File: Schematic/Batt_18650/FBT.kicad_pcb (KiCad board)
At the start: 2 copper layers, 42.8 x 122.5 mm, 19 parts, among them J1 TRRS Connector 3.5, J2 TRRS Connector 3.5, SW1 SW_SPDT

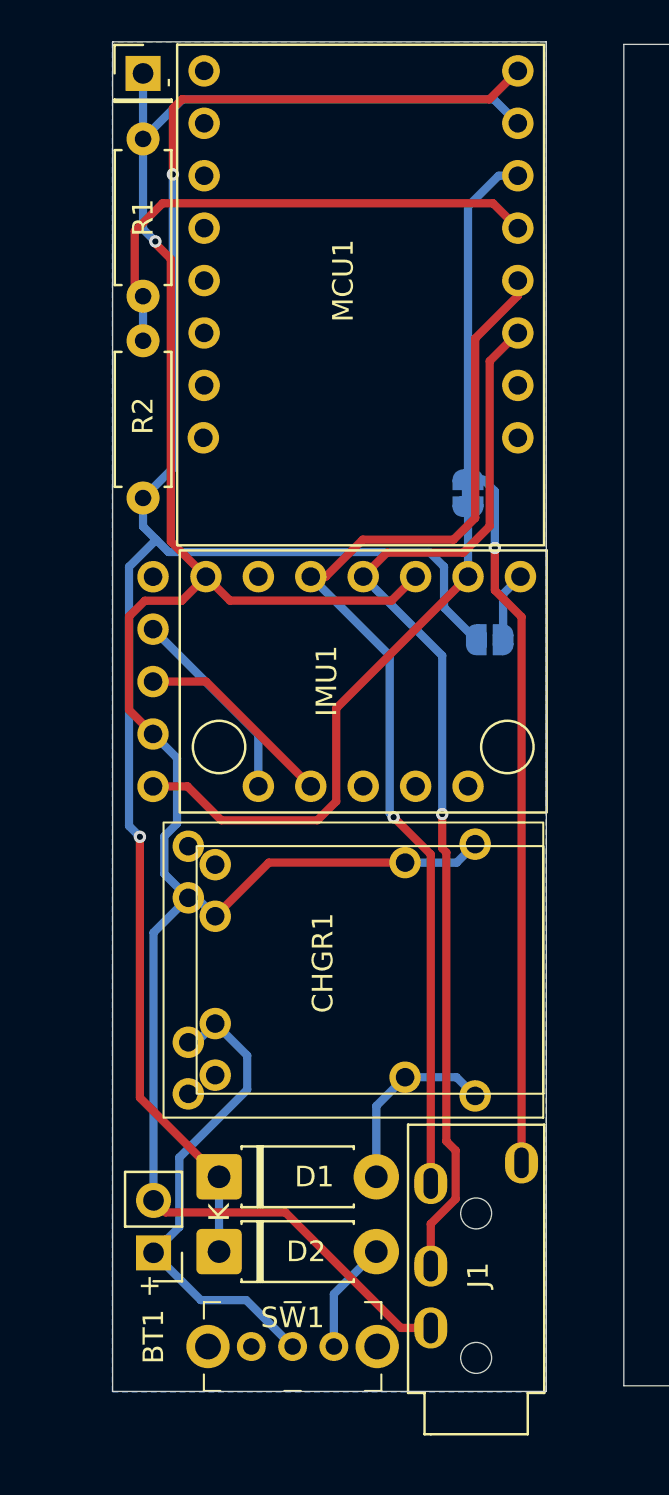
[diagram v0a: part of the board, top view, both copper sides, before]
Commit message: Update schematic to v3
Added support for a discrete LDO (HT7333) so we can correct the bodge we did with the original design.
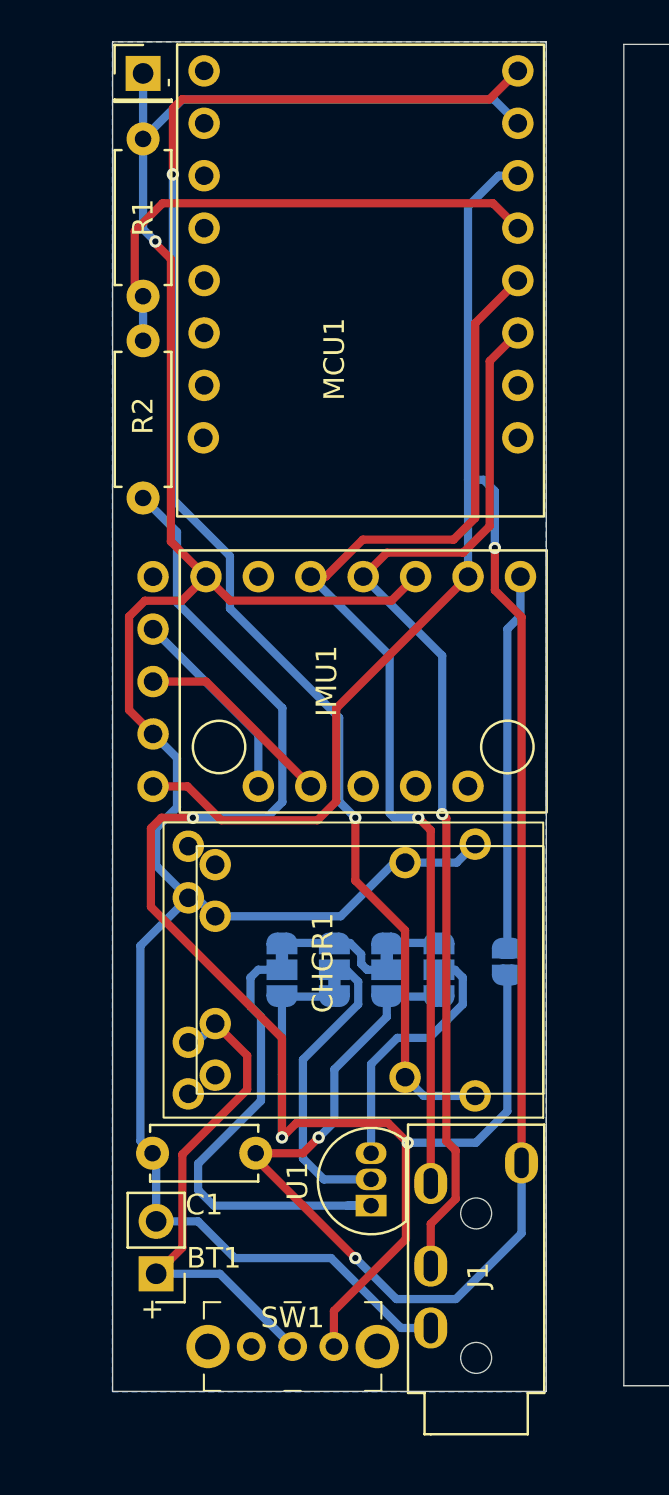
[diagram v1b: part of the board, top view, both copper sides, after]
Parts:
- removed D1: D_1N5817 / 4.8v Zener?, Diode_THT:D_DO-41_SOD81_P7.62mm_Horizontal
- removed D2: D_1N5817, Diode_THT:D_DO-41_SOD81_P7.62mm_Horizontal
- removed JP2: 3v3 in, Jumper:SolderJumper-2_P1.3mm_Bridged_RoundedPad1.0x1.5mm
- added C1: 10 uF, Capacitor_THT:C_Disc_D5.0mm_W2.5mm_P5.00mm, F.Cu at (112.0, 78.2)
- added JP3: A, Jumper:SolderJumper-3_P1.3mm_Bridged12_RoundedPad1.0x1.5mm_NumberLabels, B.Cu at (113.3, 69.3)
- added JP4: D, Jumper:SolderJumper-3_P1.3mm_Bridged12_RoundedPad1.0x1.5mm_NumberLabels, B.Cu at (120.9, 69.3)
- added JP5: B, Jumper:SolderJumper-3_P1.3mm_Bridged12_RoundedPad1.0x1.5mm_NumberLabels, B.Cu at (115.8, 69.3)
- added JP6: C, Jumper:SolderJumper-3_P1.3mm_Bridged12_RoundedPad1.0x1.5mm_NumberLabels, B.Cu at (118.4, 69.3)
- added U1: HT7333-1-TO92, Package_TO_SOT_THT:TO-92L_Inline, F.Cu at (117.6, 80.8)
- JP1: value 5v in -> E
- MCU1: footprint Espressif:ESP32-C3-Mini-V1 -> Espressif:ESP32-C3-SuperMini_PLUS
- moved JP1 15.6 mm to (124.2, 68.9), turned to -90 degrees
- moved BT1 1.02 mm to (107.2, 84.1)
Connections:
- CHGR1 pad 1: /5_VIN_LX -> ESP32_5V5
- CHGR2 pad 1: /5_VIN_LX -> ESP32_5V5
- GY1 pad 1: Net-(GY1-VIN) -> ESP32_3V3
- IMU1 pad 2: Net-(GY1-VIN) -> ESP32_3V3
- JP1 pad 2: ESP32_5V5 -> BATT_SWITCHED
- R2 pad 2: ESP32_5V5 -> BATT_SWITCHED
- SW1 pad 3: Net-(D2-A) -> BATT_SWITCHED
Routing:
- net BATT_SWITCHED: track 0.00 -> 81.6 mm, vias 0 -> 3
- net ESP32_3V3: track 70.0 -> 133.0 mm, vias 1 -> 3
- net Net-(GY1-VIN): track 26.8 -> 0.00 mm
- net /ldo_gnd: track 0.00 -> 23.3 mm
- net ESP32_5V5: track 94.8 -> 72.8 mm
- net Net-(IMU1-VIN): track 3.41 -> 18.3 mm
- net /vin: track 0.00 -> 14.8 mm
- net /vout: track 0.00 -> 12.6 mm
- net /5_VIN_LX: track 9.17 -> 0.00 mm
- net /gnd_mid: track 0.00 -> 5.89 mm
- net Net-(D2-A): track 5.45 -> 0.00 mm
- net GND: track 135.7 -> 139.6 mm
- net SDA_1: track 67.4 -> 68.1 mm
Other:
- board text added: "Type C Rev. 3.0"
- board text added: "github.com/ DrGlaucous/UFBTM"
- board text removed: "Type C Rev. 2.0"
- board text removed: "github.com/DrGlaucous/UFBTM"

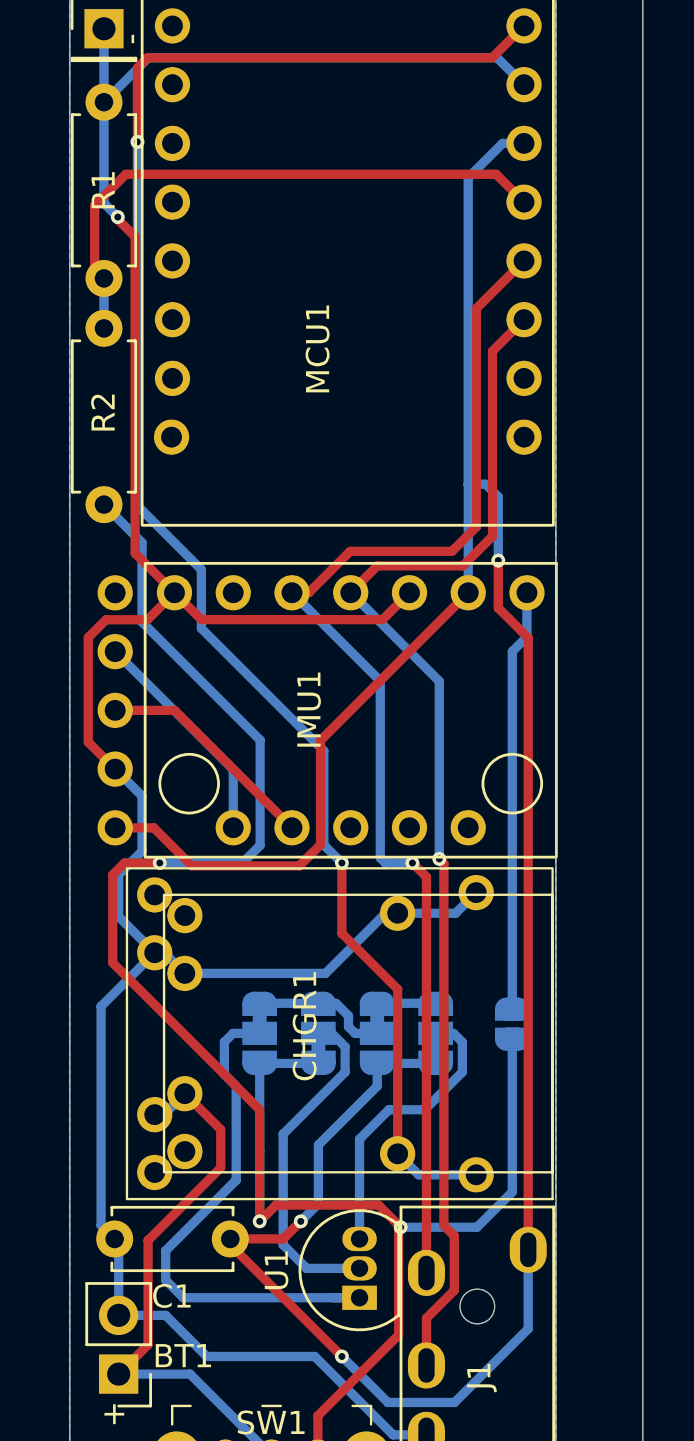
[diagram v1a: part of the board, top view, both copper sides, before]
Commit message: Slight PCB tweaking
Double-checking that everything is correct before I ship off the next batch for fabbing.
Added a jumper pad between usb-c 5v inputs.
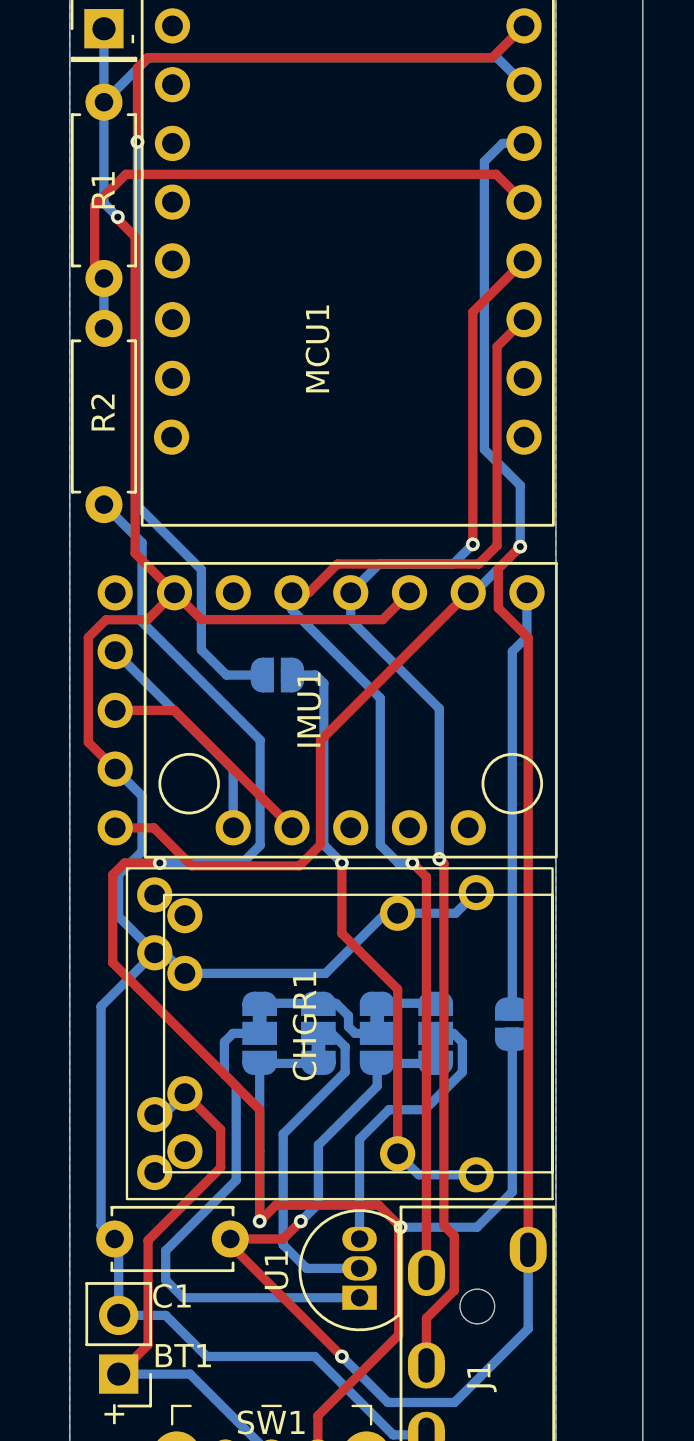
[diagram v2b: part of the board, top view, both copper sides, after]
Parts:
- added JP2: F, Jumper:SolderJumper-2_P1.3mm_Open_RoundedPad1.0x1.5mm, B.Cu at (114.0, 53.9)
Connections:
- CHGR1 pad 1: ESP32_5V5 -> Net-(CHGR1-5_VIN)
- CHGR2 pad 1: ESP32_5V5 -> Net-(CHGR1-5_VIN)
- MCU1 pad 11: SCL_1 -> SDA_1
- MCU1 pad 12: SDA_1 -> SCL_1
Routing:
- net Net-(CHGR1-5_VIN): track 0.00 -> 26.9 mm, vias 0 -> 1
- net ESP32_5V5: track 72.8 -> 46.9 mm, vias 2 -> 1
- net SCL_1: track 61.1 -> 63.3 mm, vias 1 -> 2
- net SDA_1: track 68.1 -> 66.2 mm
- net ESP32_3V3: track 133.0 -> 131.1 mm
- net /ldo_gnd: track 23.3 -> 22.1 mm
